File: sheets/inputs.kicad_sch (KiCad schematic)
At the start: 10 parts

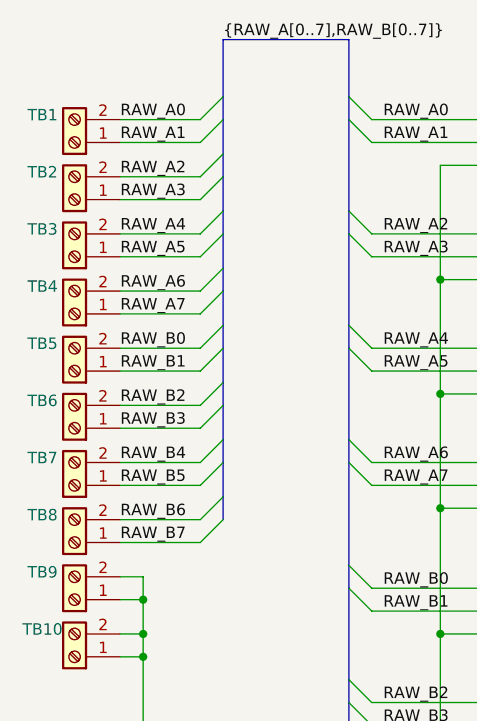
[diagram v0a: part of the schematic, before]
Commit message: add PA an PB ports
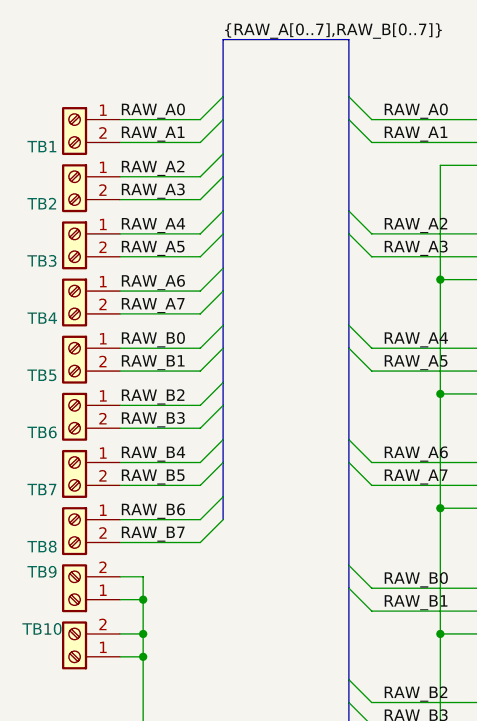
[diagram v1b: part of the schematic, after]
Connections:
- net RAW_A0: now also TB1.1 (Pin_1); no longer TB1.2 (Pin_2)
- net RAW_A1: now also TB1.2 (Pin_2); no longer TB1.1 (Pin_1)
- net RAW_A2: now also TB2.1 (Pin_1); no longer TB2.2 (Pin_2)
- net RAW_A3: now also TB2.2 (Pin_2); no longer TB2.1 (Pin_1)
- net RAW_A4: now also TB3.1 (Pin_1); no longer TB3.2 (Pin_2)
- net RAW_A5: now also TB3.2 (Pin_2); no longer TB3.1 (Pin_1)
- net RAW_A6: now also TB4.1 (Pin_1); no longer TB4.2 (Pin_2)
- net RAW_A7: now also TB4.2 (Pin_2); no longer TB4.1 (Pin_1)
- net RAW_B0: now also TB5.1 (Pin_1); no longer TB5.2 (Pin_2)
- net RAW_B1: now also TB5.2 (Pin_2); no longer TB5.1 (Pin_1)
- net RAW_B2: now also TB6.1 (Pin_1); no longer TB6.2 (Pin_2)
- net RAW_B3: now also TB6.2 (Pin_2); no longer TB6.1 (Pin_1)
- net RAW_B4: now also TB7.1 (Pin_1); no longer TB7.2 (Pin_2)
- net RAW_B5: now also TB7.2 (Pin_2); no longer TB7.1 (Pin_1)
- net RAW_B6: now also TB8.1 (Pin_1); no longer TB8.2 (Pin_2)
- net RAW_B7: now also TB8.2 (Pin_2); no longer TB8.1 (Pin_1)
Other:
- moved on the sheet: TB1, TB2, TB3, TB4, TB5, TB6, TB7, TB8
